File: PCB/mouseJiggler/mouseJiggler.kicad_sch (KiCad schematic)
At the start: 31 parts, among them J1 USB_A, J2 USB_A

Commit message: Update Schematic
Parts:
- removed C? (x4): 100n, Capacitor_SMD:C_0402_1005Metric, symbol Device:C
- removed C? (x2): 10u, Capacitor_SMD:C_0603_1608Metric, symbol Device:C
- removed C? (x2): 1u, Capacitor_SMD:C_0402_1005Metric, symbol Device:C
- removed R?: 10K, Capacitor_SMD:C_0402_1005Metric, symbol Device:R
- removed SW?: SW_Push, josh-buttons-switches:SW_Push_KMR2, symbol Switch:SW_Push
- removed U?: ATSAMD21G18A-M, Package_DFN_QFN:QFN-48-1EP_7x7mm_P0.5mm_EP5.15x5.15mm, symbol MCU_Microchip_SAMD:ATSAMD21G18A-M
- removed U?: W25Q32JVSSIQ, Package_SO:SOP-8_5.28x5.23mm_P1.27mm, symbol josh-memory:W25Q128JVSIQ
- removed Y?: Crystal, symbol Device:Crystal
- added C1, C6: 10u, Capacitor_SMD:C_0603_1608Metric, symbol Device:C
- added C14, C7: 30p, Capacitor_SMD:C_0402_1005Metric, symbol Device:C
- added C2, C4, C5: 100n, Capacitor_SMD:C_0402_1005Metric, symbol Device:C
- added C3: 1u, Capacitor_SMD:C_0402_1005Metric, symbol Device:C
- added JP1: Jumper_2_Bridged, Jumper:SolderJumper-2_P1.3mm_Bridged_RoundedPad1.0x1.5mm, symbol Jumper:Jumper_2_Bridged
- added SW1: SW_Push, josh-buttons-switches:SW_Push_KMR2, symbol Switch:SW_Push
- added U1: ATSAMD21E17A-M, Package_DFN_QFN:QFN-32-1EP_5x5mm_P0.5mm_EP3.6x3.6mm, symbol MCU_Microchip_SAMD:ATSAMD21E17A-M
- added Y1: 12MHz, Crystal:Crystal_SMD_2520-4Pin_2.5x2.0mm, symbol Device:Crystal_GND24_Small
- C11, C12: renamed from C?; value 1u -> 10u
- C13: renamed from C?; value 10u -> 100n; footprint Capacitor_SMD:C_0603_1608Metric -> Capacitor_SMD:C_0402_1005Metric
- SW2: renamed from SW?; footprint josh-buttons-switches:SW_Push_KMR2 -> josh-buttons-switches:SW_PUSH_EVQPUL_EVQPUC
- gave numbers to parts that had none: 12
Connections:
- net +3V3: now also C1.1, C2.1, C4.1, C6.1, JP1.2 (B), U1.30 (VDDIN), U1.9 (VDDANA)
- net GND: now also C8.2, C9.2, C1.2, C14.2, C2.2, C3.2, C4.2, C5.2, C6.2, C7.2, SW1.2, U1.10 (GND), U1.28 (GND), U1.33 (EP), Y1.2, Y1.4; no longer C8.1, C9.1
- net SWD_CLK: now also U1.31 (PA30)
- net SWD_IO: now also U1.32 (PA31)
- net USB_D2A+: now also U1.24 (PA25); no longer U2.2 (DP2)
- net USB_D2A-: now also U1.23 (PA24); no longer U2.1 (DM2)
- net USB_D2B+: no longer U2.16 (DP3)
- net USB_D2B-: no longer U2.15 (DM3)
- net VBUS: now also C8.1, C9.1; no longer C8.2, C9.2
- net nRESET: now also C5.1, SW1.1, U1.26 (~{RESET})
- net at U2.11 (XOUT): now also C14.1, Y1.3
- net at U2.12 (XIN): now also C7.1, Y1.1
- net D10 renamed TOGGLE
- net TOGGLE: now also U1.19 (PA18)
- net D7_LED: no longer names the net of R1.1
- net D7_LED: now also JP1.1 (A)
- new net: C3.1, U1.29 (VDDCORE)
- no-connect marks 3 -> 0
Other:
- note added: "Serial Wire Debug"
- note removed: "SPI Flash"
- note removed: "SWD"
- moved on the sheet: D1, R1

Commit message: Updated schematic
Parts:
- removed JP1: Jumper_2_Bridged, Jumper:SolderJumper-2_P1.3mm_Bridged_RoundedPad1.0x1.5mm, symbol Jumper:Jumper_2_Bridged
- removed SW1: SW_Push, josh-buttons-switches:SW_Push_KMR2, symbol Switch:SW_Push
- U2: footprint (none) -> bing-SOIC:SSOP-16_4.6x2.6mm_P0.53
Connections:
- net +3V3: now also R1.1
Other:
- moved on the sheet: C5, D1, R1

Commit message: Update crystal footprint
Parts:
- J1: footprint Connector_USB:USB_A_CNCTech_1001-011-01101_Horizontal -> bing-connector:USB_A_CNCTech_1001-011-01101_Horizontal
- J2: footprint Connector_USB:USB_A_Molex_67643_Horizontal -> bing-connector:USB_A_Molex_67643_Horizontal
- U2: footprint bing-SOIC:SSOP-16_4.6x2.6mm_P0.53 -> bing-soic:SSOP-16_4.6x2.6mm_P0.53
- Y1: footprint Crystal:Crystal_SMD_2520-4Pin_2.5x2.0mm -> bing-crystal:Crystal_SMD_2520-4Pin_2.5x2.0mm
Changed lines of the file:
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@@
       (effects (font (size 1.27 1.27)) (justify left))
     )
-    (property "Footprint" "Crystal:Crystal_SMD_2520-4Pin_2.5x2.0mm" (id 2) (at 165.1 112.395 0)
+    (property "Footprint" "bing-crystal:Crystal_SMD_2520-4Pin_2.5x2.0mm" (id 2) (at 165.1 112.395 0)
       (effects (font (size 1.27 1.27)) hide)
     )
@@
     (property "Reference" "J1" (id 0) (at 125.857 41.7534 0))
     (property "Value" "USB_A" (id 1) (at 125.857 44.5285 0))
-    (property "Footprint" "Connector_USB:USB_A_CNCTech_1001-011-01101_Horizontal" (id 2) (at 128.27 54.61 0)
+    (property "Footprint" "bing-connector:USB_A_CNCTech_1001-011-01101_Horizontal" (id 2) (at 128.27 54.61 0)
       (effects (font (size 1.27 1.27)) hide)
     )
@@
     (property "Reference" "J2" (id 0) (at 179.832 42.3884 0))
     (property "Value" "USB_A" (id 1) (at 179.832 45.1635 0))
-    (property "Footprint" "Connector_USB:USB_A_Molex_67643_Horizontal" (id 2) (at 182.245 55.245 0)
+    (property "Footprint" "bing-connector:USB_A_Molex_67643_Horizontal" (id 2) (at 182.245 55.245 0)
       (effects (font (size 1.27 1.27)) hide)
     )
@@
     (property "Reference" "U2" (id 0) (at 139.065 94.5092 0))
     (property "Value" "SL2.1S" (id 1) (at 139.065 97.2843 0))
-    (property "Footprint" "bing-SOIC:SSOP-16_4.6x2.6mm_P0.53" (id 2) (at 132.715 93.345 0)
+    (property "Footprint" "bing-soic:SSOP-16_4.6x2.6mm_P0.53" (id 2) (at 132.715 93.345 0)
       (effects (font (size 1.27 1.27)) hide)
     )
@@
     )
     (path "/93a84665-3653-4eb7-b7bf-a135aaf7cb3a"
-      (reference "J1") (unit 1) (value "USB_A") (footprint "Connector_USB:USB_A_CNCTech_1001-011-01101_Horizontal")
+      (reference "J1") (unit 1) (value "USB_A") (footprint "bing-connector:USB_A_CNCTech_1001-011-01101_Horizontal")
     )
     (path "/2b386749-9e2d-4da3-941c-958b4e64e0c4"
-      (reference "J2") (unit 1) (value "USB_A") (footprint "Connector_USB:USB_A_Molex_67643_Horizontal")
+      (reference "J2") (unit 1) (value "USB_A") (footprint "bing-connector:USB_A_Molex_67643_Horizontal")
     )
     (path "/e3e22f97-0fe4-42d4-8b68-5b1ee1d2ecff"
@@
     )
     (path "/731b5413-69a5-454f-9864-2b85f7c7a784"
-      (reference "U2") (unit 1) (value "SL2.1S") (footprint "bing-SOIC:SSOP-16_4.6x2.6mm_P0.53")
+      (reference "U2") (unit 1) (value "SL2.1S") (footprint "bing-soic:SSOP-16_4.6x2.6mm_P0.53")
     )
     (path "/2cd5858d-046d-483a-bfeb-7cd2581215d7"
@@
     )
     (path "/242cb84a-3ae3-41c5-a92a-9bafb662ffd8"
-      (reference "Y1") (unit 1) (value "12MHz") (footprint "Crystal:Crystal_SMD_2520-4Pin_2.5x2.0mm")
-    )
-  )
+      (reference "Y1") (unit 1) (value "12MHz") (footprint "bing-crystal:Crystal_SMD_2520-4Pin_2.5x2.0mm")
+    )
+  )

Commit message: Update PCB
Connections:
- net USB_D2A+ is gone; now on net USB_JIG+: U1.24 (PA25)
- net USB_D2A- is gone; now on net USB_JIG-: U1.23 (PA24)
- net USB_D2B+ is gone; now on net USB_OUT+: J2.3 (D+)
- net USB_D2B- is gone; now on net USB_OUT-: J2.2 (D-)
- net TOGGLE: now also U1.2 (PA01); no longer U1.19 (PA18)
- net USB_JIG+: now also U2.16 (DP3)
- net USB_JIG-: now also U2.15 (DM3)
- net USB_OUT+: now also U2.2 (DP2)
- net USB_OUT-: now also U2.1 (DM2)
- no-connect marks 0 -> 25
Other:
- note added: "Power LED"
- note removed: "Test LED"
- moved on the sheet: SW2
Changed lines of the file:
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@@
   (junction (at 259.715 48.895) (diameter 1.016) (color 0 0 0 0))
   (junction (at 260.35 104.775) (diameter 1.016) (color 0 0 0 0))
+  (no_connect (at 69.215 76.835))
+  (no_connect (at 69.215 81.915))
+  (no_connect (at 69.215 84.455))
+  (no_connect (at 69.215 86.995))
+  (no_connect (at 69.215 89.535))
+  (no_connect (at 69.215 92.075))
+  (no_connect (at 69.215 94.615))
+  (no_connect (at 69.215 97.155))
+  (no_connect (at 69.215 99.695))
+  (no_connect (at 69.215 102.235))
+  (no_connect (at 69.215 104.775))
+  (no_connect (at 69.215 112.395))
+  (no_connect (at 69.215 114.935))
+  (no_connect (at 69.215 117.475))
+  (no_connect (at 69.215 120.015))
+  (no_connect (at 69.215 122.555))
+  (no_connect (at 69.215 125.095))
+  (no_connect (at 69.215 132.715))
+  (no_connect (at 69.215 135.255))
+  (no_connect (at 69.215 145.415))
+  (no_connect (at 69.215 147.955))
+  (no_connect (at 128.905 106.045))
+  (no_connect (at 128.905 108.585))
+  (no_connect (at 149.225 106.045))
+  (no_connect (at 149.225 108.585))
   (wire (pts (xy 23.495 55.245) (xy 23.495 56.515))
     (stroke (width 0) (type solid) (color 0 0 0 0))
@@
     (stroke (width 0) (type solid) (color 0 0 0 0))
   )
-  (wire (pts (xy 69.215 122.555) (xy 81.28 122.555))
+  (wire (pts (xy 69.215 79.375) (xy 81.28 79.375))
     (stroke (width 0) (type solid) (color 0 0 0 0))
   )
@@
     (stroke (width 0) (type solid) (color 0 0 0 0))
   )
+  (wire (pts (xy 106.68 170.18) (xy 106.68 162.56))
+    (stroke (width 0) (type solid) (color 0 0 0 0))
+  )
+  (wire (pts (xy 106.68 180.34) (xy 106.68 184.785))
+    (stroke (width 0) (type solid) (color 0 0 0 0))
+  )
   (wire (pts (xy 111.76 114.935) (xy 111.76 116.205))
     (stroke (width 0) (type solid) (color 0 0 0 0))
@@
     (stroke (width 0) (type solid) (color 0 0 0 0))
   )
-  (wire (pts (xy 114.3 170.18) (xy 114.3 162.56))
-    (stroke (width 0) (type solid) (color 0 0 0 0))
-  )
-  (wire (pts (xy 114.3 180.34) (xy 114.3 184.785))
-    (stroke (width 0) (type solid) (color 0 0 0 0))
-  )
-  (wire (pts (xy 116.205 100.965) (xy 127 100.965))
-    (stroke (width 0) (type solid) (color 0 0 0 0))
-  )
-  (wire (pts (xy 116.205 103.505) (xy 127 103.505))
-    (stroke (width 0) (type solid) (color 0 0 0 0))
-  )
   (wire (pts (xy 116.84 116.205) (xy 128.905 116.205))
     (stroke (width 0) (type solid) (color 0 0 0 0))
@@
     (stroke (width 0) (type solid) (color 0 0 0 0))
   )
+  (wire (pts (xy 128.905 100.965) (xy 118.11 100.965))
+    (stroke (width 0) (type solid) (color 0 0 0 0))
+  )
+  (wire (pts (xy 128.905 103.505) (xy 118.11 103.505))
+    (stroke (width 0) (type solid) (color 0 0 0 0))
+  )
   (wire (pts (xy 128.905 111.125) (xy 118.11 111.125))
     (stroke (width 0) (type solid) (color 0 0 0 0))
@@
     (stroke (width 0) (type solid) (color 0 0 0 0))
   )
-  (wire (pts (xy 151.765 100.965) (xy 162.56 100.965))
-    (stroke (width 0) (type solid) (color 0 0 0 0))
-  )
-  (wire (pts (xy 151.765 103.505) (xy 162.56 103.505))
-    (stroke (width 0) (type solid) (color 0 0 0 0))
-  )
   (wire (pts (xy 156.21 48.26) (xy 160.02 48.26))
     (stroke (width 0) (type solid) (color 0 0 0 0))
@@
   )
   (wire (pts (xy 160.02 45.72) (xy 160.02 48.26))
+    (stroke (width 0) (type solid) (color 0 0 0 0))
+  )
+  (wire (pts (xy 160.02 100.965) (xy 149.225 100.965))
+    (stroke (width 0) (type solid) (color 0 0 0 0))
+  )
+  (wire (pts (xy 160.02 103.505) (xy 149.225 103.505))
     (stroke (width 0) (type solid) (color 0 0 0 0))
   )
@@
     (effects (font (size 3 3)) (justify right bottom))
   )
-  (text "Toggle" (at 107.315 160.02 0)
+  (text "Toggle" (at 99.695 160.02 0)
     (effects (font (size 3 3)) (justify left bottom))
   )
-  (text "Test LED" (at 127 160.02 0)
+  (text "Power LED" (at 123.825 160.02 0)
     (effects (font (size 3 3)) (justify left bottom))
   )
@@
     (effects (font (size 3 3)) (justify right bottom))
   )
-  (label "USB_D2A-" (at 80.01 137.795 180)
-    (effects (font (size 1.27 1.27)) (justify right bottom))
-  )
-  (label "USB_D2A+" (at 80.01 140.335 180)
-    (effects (font (size 1.27 1.27)) (justify right bottom))
-  )
-  (label "TOGGLE" (at 81.28 122.555 180)
+  (label "USB_JIG-" (at 80.01 137.795 180)
+    (effects (font (size 1.27 1.27)) (justify right bottom))
+  )
+  (label "USB_JIG+" (at 80.01 140.335 180)
+    (effects (font (size 1.27 1.27)) (justify right bottom))
+  )
+  (label "TOGGLE" (at 81.28 79.375 180)
     (effects (font (size 1.27 1.27)) (justify right bottom))
   )
@@
     (effects (font (size 1.27 1.27)) (justify right bottom))
   )
-  (label "TOGGLE" (at 114.3 162.56 270)
-    (effects (font (size 1.27 1.27)) (justify right bottom))
-  )
-  (label "USB_JIG-" (at 116.205 100.965 0)
+  (label "TOGGLE" (at 106.68 162.56 270)
+    (effects (font (size 1.27 1.27)) (justify right bottom))
+  )
+  (label "USB_OUT-" (at 118.11 100.965 0)
     (effects (font (size 1.27 1.27)) (justify left bottom))
   )
-  (label "USB_JIG+" (at 116.205 103.505 0)
+  (label "USB_OUT+" (at 118.11 103.505 0)
     (effects (font (size 1.27 1.27)) (justify left bottom))
   )
@@
     (effects (font (size 1.27 1.27)) (justify right bottom))
   )
-  (label "USB_OUT+" (at 162.56 100.965 180)
-    (effects (font (size 1.27 1.27)) (justify right bottom))
-  )
-  (label "USB_OUT-" (at 162.56 103.505 180)
-    (effects (font (size 1.27 1.27)) (justify right bottom))
-  )
-  (label "USB_D2B+" (at 196.85 53.975 180)
-    (effects (font (size 1.27 1.27)) (justify right bottom))
-  )
-  (label "USB_D2B-" (at 196.85 56.515 180)
+  (label "USB_JIG+" (at 160.02 100.965 180)
+    (effects (font (size 1.27 1.27)) (justify right bottom))
+  )
+  (label "USB_JIG-" (at 160.02 103.505 180)
+    (effects (font (size 1.27 1.27)) (justify right bottom))
+  )
+  (label "USB_OUT+" (at 196.85 53.975 180)
+    (effects (font (size 1.27 1.27)) (justify right bottom))
+  )
+  (label "USB_OUT-" (at 196.85 56.515 180)
     (effects (font (size 1.27 1.27)) (justify right bottom))
   )
@@
     (pin "1")
   )
+  (symbol (lib_id "power:GND") (at 106.68 184.785 0) (unit 1)
+    (in_bom yes) (on_board yes) (fields_autoplaced)
+    (property "Reference" "#PWR0132" (id 0) (at 106.68 191.135 0)
+      (effects (font (size 1.27 1.27)) hide)
+    )
+    (property "Value" "GND" (id 1) (at 106.68 189.1094 0))
+    (property "Footprint" "" (id 2) (at 106.68 184.785 0)
+      (effects (font (size 1.27 1.27)) hide)
+    )
+    (property "Datasheet" "" (id 3) (at 106.68 184.785 0)
+      (effects (font (size 1.27 1.27)) hide)
+    )
+    (pin "1")
+  )
   (symbol (lib_id "power:GND") (at 111.76 125.095 0) (unit 1)
     (in_bom yes) (on_board yes) (fields_autoplaced)
@@
     )
     (property "Datasheet" "" (id 3) (at 111.76 125.095 0)
-      (effects (font (size 1.27 1.27)) hide)
-    )
-    (pin "1")
-  )
-  (symbol (lib_id "power:GND") (at 114.3 184.785 0) (unit 1)
-    (in_bom yes) (on_board yes) (fields_autoplaced)
-    (property "Reference" "#PWR0132" (id 0) (at 114.3 191.135 0)
-      (effects (font (size 1.27 1.27)) hide)
-    )
-    (property "Value" "GND" (id 1) (at 114.3 189.1094 0))
-    (property "Footprint" "" (id 2) (at 114.3 184.785 0)
-      (effects (font (size 1.27 1.27)) hide)
-    )
-    (property "Datasheet" "" (id 3) (at 114.3 184.785 0)
       (effects (font (size 1.27 1.27)) hide)
     )
@@
     (pin "2")
   )
-  (symbol (lib_id "Switch:SW_Push") (at 114.3 175.26 270) (unit 1)
-    (in_bom yes) (on_board yes) (fields_autoplaced)
-    (property "Reference" "SW2" (id 0) (at 117.9831 174.4991 90)
-      (effects (font (size 1.27 1.27)) (justify left))
-    )
-    (property "Value" "SW_Push" (id 1) (at 117.9831 176.7978 90)
-      (effects (font (size 1.27 1.27)) (justify left))
-    )
-    (property "Footprint" "josh-buttons-switches:SW_PUSH_EVQPUL_EVQPUC" (id 2) (at 119.38 175.26 0)
-      (effects (font (size 1.27 1.27)) hide)
-    )
-    (property "Datasheet" "~" (id 3) (at 119.38 175.26 0)
-      (effects (font (size 1.27 1.27)) hide)
-    )
+  (symbol (lib_id "Switch:SW_Push") (at 106.68 175.26 270) (unit 1)
+    (in_bom yes) (on_board yes) (fields_autoplaced)
+    (property "Reference" "SW2" (id 0) (at 110.3631 174.4991 90)
+      (effects (font (size 1.27 1.27)) (justify left))
+    )
+    (property "Value" "SW_Push" (id 1) (at 110.3631 176.7978 90)
+      (effects (font (size 1.27 1.27)) (justify left))
+    )
+    (property "Footprint" "josh-buttons-switches:SW_PUSH_EVQPUL_EVQPUC" (id 2) (at 111.76 175.26 0)
+      (effects (font (size 1.27 1.27)) hide)
+    )
+    (property "Datasheet" "~" (id 3) (at 111.76 175.26 0)
+      (effects (font (size 1.27 1.27)) hide)
+    )

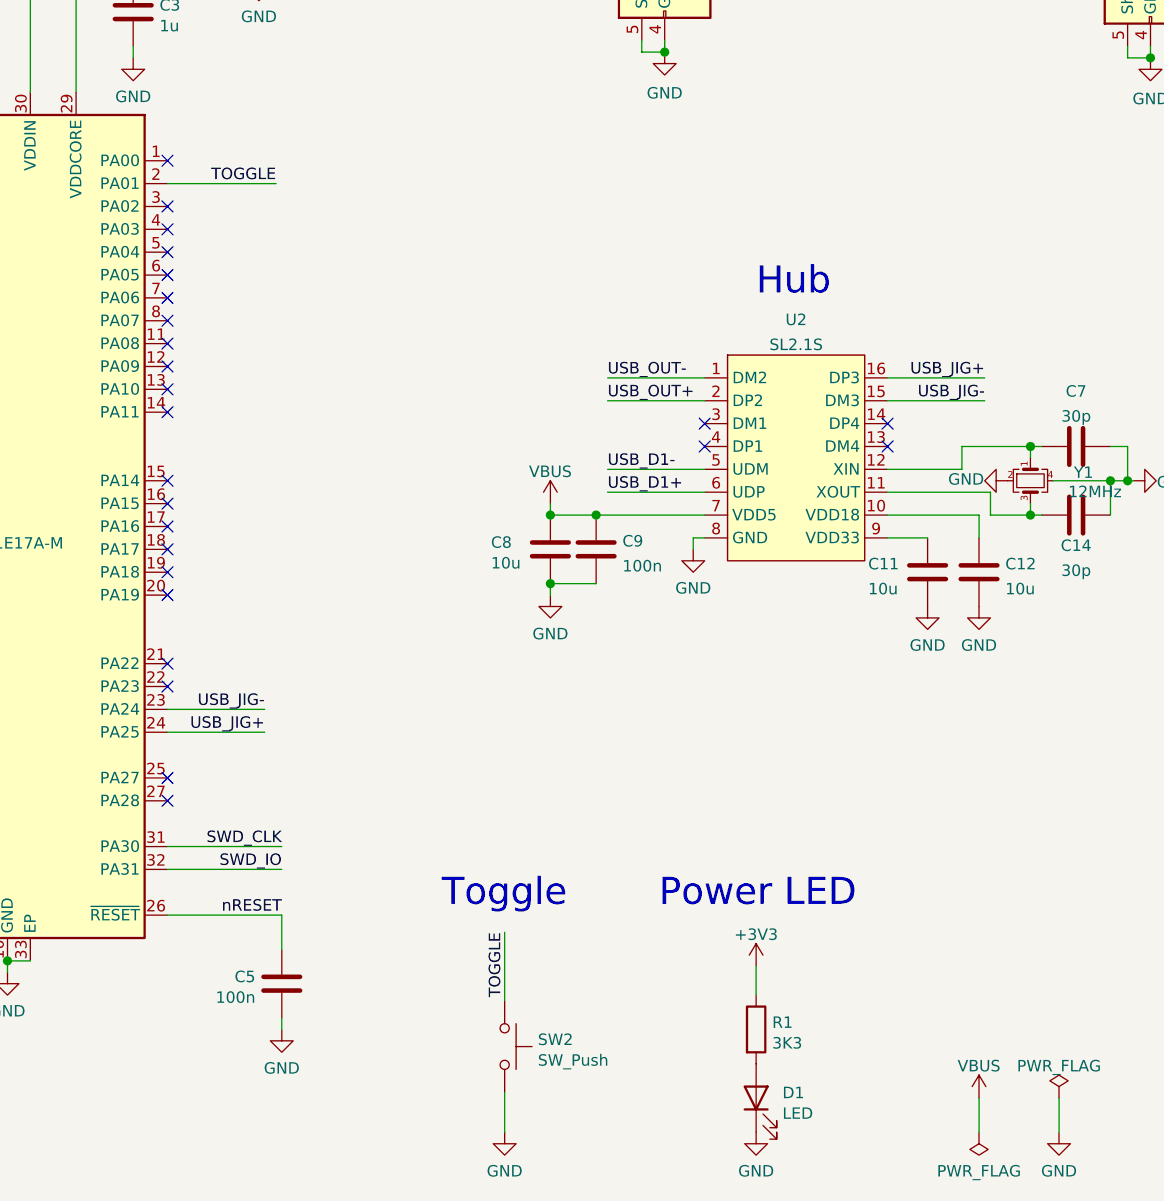
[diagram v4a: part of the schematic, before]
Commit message: Added test LED and updated PCB
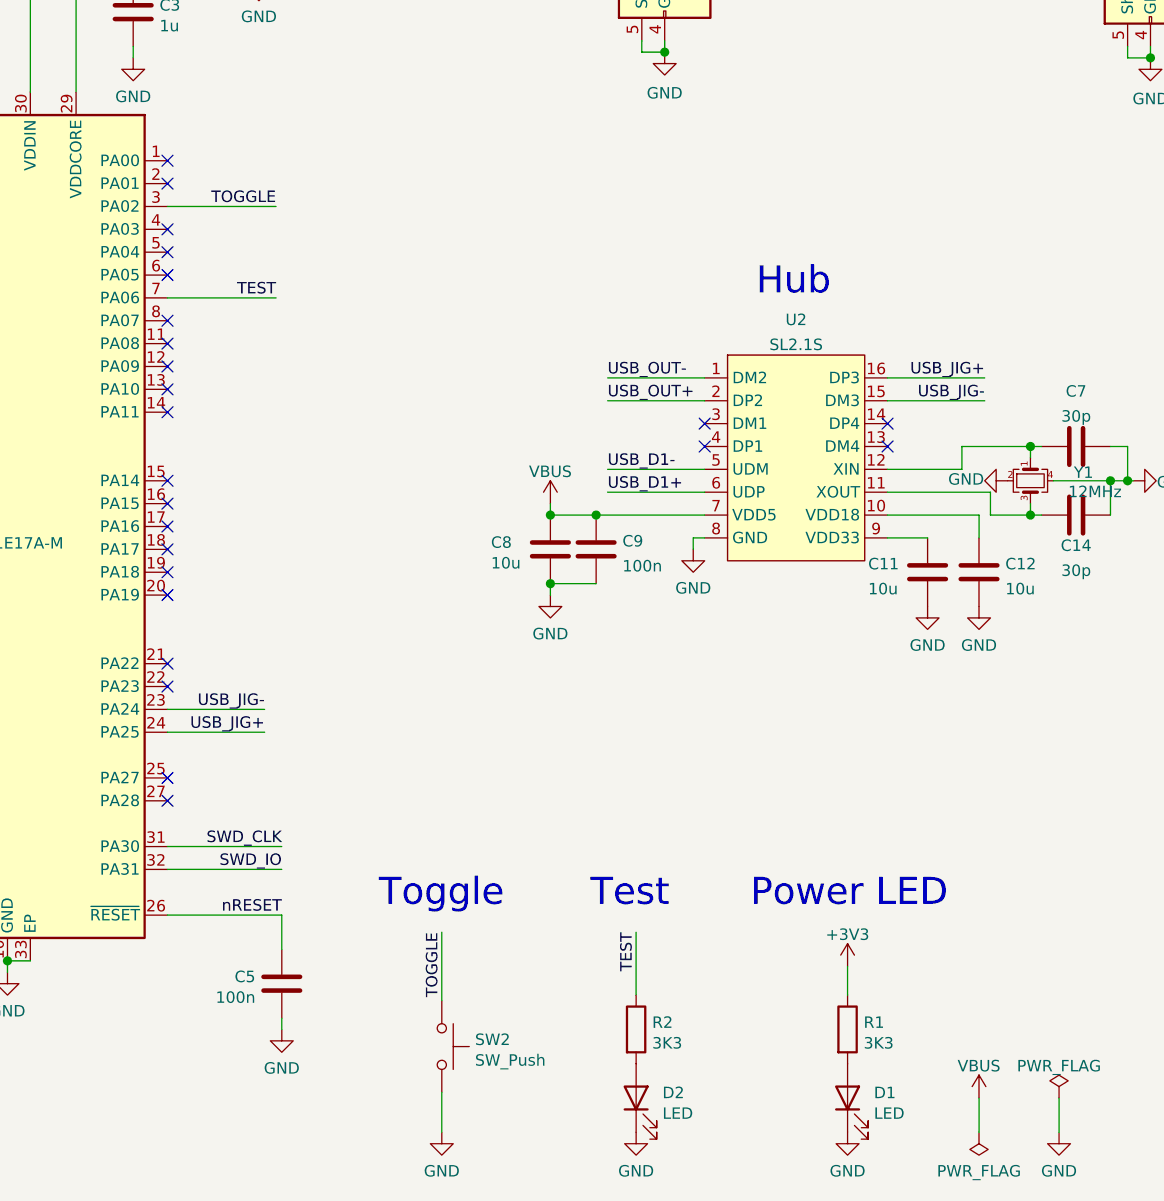
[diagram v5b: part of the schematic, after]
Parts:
- added D2: LED, LED_SMD:LED_0603_1608Metric, symbol Device:LED
- added R2: 3K3, Capacitor_SMD:C_0402_1005Metric, symbol Device:R
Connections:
- net GND: now also D2.1 (K)
- net TOGGLE: now also U1.3 (PA02); no longer U1.2 (PA01)
- net TEST: now reaches U1.7 (PA06)
- net TEST: now also R2.1
- new net: D2.2 (A), R2.2
- no-connect marks 25 -> 24
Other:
- note added: "Test"
- moved on the sheet: D1, R1, SW2
